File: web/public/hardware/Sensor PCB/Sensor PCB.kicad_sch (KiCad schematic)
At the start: 27 parts, among them J1 Conn_01x08_Pin, J2 Conn_01x08_Pin, J3 Conn_01x02_Pin, J4 Conn_01x02_Pin, U1 DRV5033AJxDBZ, U2 DRV5033AJxDBZ, U3 DRV5033AJxDBZ, U4 DRV5033AJxDBZ, U5 74LS11, U6 74LS11

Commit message: Fix routing to fit hall effect decoupling capacitors
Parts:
- added C3, C4, C5, C6: 0.1uF, Capacitor_SMD:C_0805_2012Metric_Pad1.18x1.45mm_HandSolder, symbol Device:C
- added H4: MountingHole, MountingHole:MountingHole_2.7mm_M2.5, symbol Mechanical:MountingHole
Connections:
- net +5V: now also C3.1, C4.1, C5.1, C6.1
- net GND: now also C3.2, C4.2, C5.2, C6.2
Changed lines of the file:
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@@
     (company "ECE 477")
   )
+  (junction (at 111.76 101.6) (diameter 0) (color 0 0 0 0)
+  )
+  (junction (at 60.96 55.88) (diameter 0) (color 0 0 0 0)
+  )
   (junction (at 237.49 120.65) (diameter 0) (color 0 0 0 0)
   )
@@
   (junction (at 123.19 111.76) (diameter 0) (color 0 0 0 0)
   )
+  (junction (at 59.69 101.6) (diameter 0) (color 0 0 0 0)
+  )
   (junction (at 237.49 146.05) (diameter 0) (color 0 0 0 0)
   )
@@
   )
   (junction (at 177.8 128.27) (diameter 0) (color 0 0 0 0)
+  )
+  (junction (at 110.49 55.88) (diameter 0) (color 0 0 0 0)
   )
   (junction (at 203.2 121.92) (diameter 0) (color 0 0 0 0)
@@
     (stroke (width 0) (type default))
   )
+  (wire (pts (xy 96.52 55.88) (xy 110.49 55.88))
+    (stroke (width 0) (type default))
+  )
   (wire (pts (xy 251.46 69.85) (xy 241.3 69.85))
     (stroke (width 0) (type default))
@@
     (stroke (width 0) (type default))
   )
+  (wire (pts (xy 45.72 101.6) (xy 59.69 101.6))
+    (stroke (width 0) (type default))
+  )
   (wire (pts (xy 123.19 66.04) (xy 123.19 81.28))
     (stroke (width 0) (type default))
@@
     (stroke (width 0) (type default))
   )
+  (wire (pts (xy 45.72 55.88) (xy 60.96 55.88))
+    (stroke (width 0) (type default))
+  )
   (wire (pts (xy 128.27 93.98) (xy 128.27 129.54))
     (stroke (width 0) (type default))
@@
   )
   (wire (pts (xy 69.85 111.76) (xy 69.85 93.98))
+    (stroke (width 0) (type default))
+  )
+  (wire (pts (xy 96.52 101.6) (xy 111.76 101.6))
     (stroke (width 0) (type default))
   )
@@
   (label "COL2_OUT" (at 153.67 81.28 0) (fields_autoplaced)
     (effects (font (size 1.27 1.27)) (justify left bottom))
+  )
+  (symbol (lib_id "power:GND") (at 96.52 109.22 0) (unit 1)
+    (in_bom yes) (on_board yes) (dnp no) (fields_autoplaced)
+    (property "Reference" "#PWR029" (at 96.52 115.57 0)
+      (effects (font (size 1.27 1.27)) hide)
+    )
+    (property "Value" "GND" (at 96.52 114.3 0)
+      (effects (font (size 1.27 1.27)) hide)
+    )
+    (property "Footprint" "" (at 96.52 109.22 0)
+      (effects (font (size 1.27 1.27)) hide)
+    )
+    (property "Datasheet" "" (at 96.52 109.22 0)
+      (effects (font (size 1.27 1.27)) hide)
+    )
+    (pin "1")
+    (instances
+      (project "Sensor PCB"
+        (path "/a9f063f9-73a8-44d6-aee6-f41a657d12c2"
+          (reference "#PWR029") (unit 1)
+        )
+      )
+    )
   )
   (symbol (lib_id "power:+5V") (at 73.66 55.88 0) (unit 1)
@@
     )
   )
+  (symbol (lib_id "Device:C") (at 45.72 59.69 0) (unit 1)
+    (in_bom yes) (on_board yes) (dnp no) (fields_autoplaced)
+    (property "Reference" "C4" (at 49.53 58.42 0)
+      (effects (font (size 1.27 1.27)) (justify left))
+    )
+    (property "Value" "0.1uF" (at 49.53 60.96 0)
+      (effects (font (size 1.27 1.27)) (justify left))
+    )
+    (property "Footprint" "Capacitor_SMD:C_0805_2012Metric_Pad1.18x1.45mm_HandSolder" (at 46.6852 63.5 0)
+      (effects (font (size 1.27 1.27)) hide)
+    )
+    (property "Datasheet" "~" (at 45.72 59.69 0)
+      (effects (font (size 1.27 1.27)) hide)
+    )
+    (pin "1")
+    (pin "2")
+    (instances
+      (project "Sensor PCB"
+        (path "/a9f063f9-73a8-44d6-aee6-f41a657d12c2"
+          (reference "C4") (unit 1)
+        )
+      )
+    )
+  )
   (symbol (lib_id "LED:WS2812B") (at 180.34 60.96 0) (unit 1)
     (in_bom yes) (on_board yes) (dnp no) (fields_autoplaced)
@@
         (path "/a9f063f9-73a8-44d6-aee6-f41a657d12c2"
           (reference "D1") (unit 1)
+        )
+      )
+    )
+  )
+  (symbol (lib_id "Device:C") (at 45.72 105.41 0) (unit 1)
+    (in_bom yes) (on_board yes) (dnp no) (fields_autoplaced)
+    (property "Reference" "C3" (at 49.53 104.14 0)
+      (effects (font (size 1.27 1.27)) (justify left))
+    )
+    (property "Value" "0.1uF" (at 49.53 106.68 0)
+      (effects (font (size 1.27 1.27)) (justify left))
+    )
+    (property "Footprint" "Capacitor_SMD:C_0805_2012Metric_Pad1.18x1.45mm_HandSolder" (at 46.6852 109.22 0)
+      (effects (font (size 1.27 1.27)) hide)
+    )
+    (property "Datasheet" "~" (at 45.72 105.41 0)
+      (effects (font (size 1.27 1.27)) hide)
+    )
+    (pin "1")
+    (pin "2")
+    (instances
+      (project "Sensor PCB"
+        (path "/a9f063f9-73a8-44d6-aee6-f41a657d12c2"
+          (reference "C3") (unit 1)
+        )
+      )
+    )
+  )
+  (symbol (lib_id "power:GND") (at 96.52 63.5 0) (unit 1)
+    (in_bom yes) (on_board yes) (dnp no) (fields_autoplaced)
+    (property "Reference" "#PWR040" (at 96.52 69.85 0)
+      (effects (font (size 1.27 1.27)) hide)
+    )
+    (property "Value" "GND" (at 96.52 68.58 0)
+      (effects (font (size 1.27 1.27)) hide)
+    )
+    (property "Footprint" "" (at 96.52 63.5 0)
+      (effects (font (size 1.27 1.27)) hide)
+    )
+    (property "Datasheet" "" (at 96.52 63.5 0)
+      (effects (font (size 1.27 1.27)) hide)
+    )
+    (pin "1")
+    (instances
+      (project "Sensor PCB"
+        (path "/a9f063f9-73a8-44d6-aee6-f41a657d12c2"
+          (reference "#PWR040") (unit 1)
         )
       )
@@
     )
   )
+  (symbol (lib_id "Mechanical:MountingHole") (at 38.1 191.77 0) (unit 1)
+    (in_bom yes) (on_board yes) (dnp no) (fields_autoplaced)
+    (property "Reference" "H4" (at 40.64 190.5 0)
+      (effects (font (size 1.27 1.27)) (justify left))
+    )
+    (property "Value" "MountingHole" (at 40.64 193.04 0)
+      (effects (font (size 1.27 1.27)) (justify left))
+    )
+    (property "Footprint" "MountingHole:MountingHole_2.7mm_M2.5" (at 38.1 191.77 0)
+      (effects (font (size 1.27 1.27)) hide)
+    )
+    (property "Datasheet" "~" (at 38.1 191.77 0)
+      (effects (font (size 1.27 1.27)) hide)
+    )
+    (instances
+      (project "Sensor PCB"
+        (path "/a9f063f9-73a8-44d6-aee6-f41a657d12c2"
+          (reference "H4") (unit 1)
+        )
+      )
+    )
+  )
+  (symbol (lib_id "power:GND") (at 45.72 63.5 0) (unit 1)
+    (in_bom yes) (on_board yes) (dnp no) (fields_autoplaced)
+    (property "Reference" "#PWR039" (at 45.72 69.85 0)
+      (effects (font (size 1.27 1.27)) hide)
+    )
+    (property "Value" "GND" (at 45.72 68.58 0)
+      (effects (font (size 1.27 1.27)) hide)
+    )
+    (property "Footprint" "" (at 45.72 63.5 0)
+      (effects (font (size 1.27 1.27)) hide)
+    )
+    (property "Datasheet" "" (at 45.72 63.5 0)
+      (effects (font (size 1.27 1.27)) hide)
+    )
+    (pin "1")
+    (instances
+      (project "Sensor PCB"
+        (path "/a9f063f9-73a8-44d6-aee6-f41a657d12c2"
+          (reference "#PWR039") (unit 1)
+        )
+      )
+    )
+  )
   (symbol (lib_id "power:+5V") (at 110.49 55.88 0) (unit 1)
     (in_bom yes) (on_board yes) (dnp no) (fields_autoplaced)
@@
     )
   )
+  (symbol (lib_id "Device:C") (at 96.52 59.69 0) (unit 1)
+    (in_bom yes) (on_board yes) (dnp no) (fields_autoplaced)
+    (property "Reference" "C5" (at 100.33 58.42 0)
+      (effects (font (size 1.27 1.27)) (justify left))
+    )
+    (property "Value" "0.1uF" (at 100.33 60.96 0)
+      (effects (font (size 1.27 1.27)) (justify left))
+    )
+    (property "Footprint" "Capacitor_SMD:C_0805_2012Metric_Pad1.18x1.45mm_HandSolder" (at 97.4852 63.5 0)
+      (effects (font (size 1.27 1.27)) hide)
+    )
+    (property "Datasheet" "~" (at 96.52 59.69 0)
+      (effects (font (size 1.27 1.27)) hide)
+    )
+    (pin "1")
+    (pin "2")
+    (instances
+      (project "Sensor PCB"
+        (path "/a9f063f9-73a8-44d6-aee6-f41a657d12c2"
+          (reference "C5") (unit 1)
+        )
+      )
+    )
+  )
   (symbol (lib_id "power:+5V") (at 251.46 59.69 90) (mirror x) (unit 1)
     (in_bom yes) (on_board yes) (dnp no) (fields_autoplaced)
@@
     )
   )
+  (symbol (lib_id "power:GND") (at 45.72 109.22 0) (unit 1)
+    (in_bom yes) (on_board yes) (dnp no) (fields_autoplaced)
+    (property "Reference" "#PWR030" (at 45.72 115.57 0)
+      (effects (font (size 1.27 1.27)) hide)
+    )
+    (property "Value" "GND" (at 45.72 114.3 0)
+      (effects (font (size 1.27 1.27)) hide)
+    )
+    (property "Footprint" "" (at 45.72 109.22 0)
+      (effects (font (size 1.27 1.27)) hide)
+    )
+    (property "Datasheet" "" (at 45.72 109.22 0)
+      (effects (font (size 1.27 1.27)) hide)
+    )
+    (pin "1")
+    (instances
+      (project "Sensor PCB"
+        (path "/a9f063f9-73a8-44d6-aee6-f41a657d12c2"
+          (reference "#PWR030") (unit 1)
+        )
+      )
+    )
+  )
   (symbol (lib_id "power:GND") (at 60.96 76.2 0) (unit 1)
     (in_bom yes) (on_board yes) (dnp no) (fields_autoplaced)
@@
         )
       )
+    )
+  )
+  (symbol (lib_id "Device:C") (at 96.52 105.41 0) (unit 1)
+    (in_bom yes) (on_board yes) (dnp no) (fields_autoplaced)
+    (property "Reference" "C6" (at 100.33 104.14 0)
+      (effects (font (size 1.27 1.27)) (justify left))
+    )
+    (property "Value" "0.1uF" (at 100.33 106.68 0)
+      (effects (font (size 1.27 1.27)) (justify left))
+    )
+    (property "Footprint" "Capacitor_SMD:C_0805_2012Metric_Pad1.18x1.45mm_HandSolder" (at 97.4852 109.22 0)
+      (effects (font (size 1.27 1.27)) hide)
+    )
+    (property "Datasheet" "~" (at 96.52 105.41 0)
+      (effects (font (size 1.27 1.27)) hide)
+    )
+    (pin "1")
+    (pin "2")
+    (instances
+      (project "Sensor PCB"
+        (path "/a9f063f9-73a8-44d6-aee6-f41a657d12c2"
+          (reference "C6") (unit 1)
+        )
+      )

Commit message: Flip LED2 signal direction
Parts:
- renumbered D4 to D3, D3 to D4
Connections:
- net LED2_IN: now also J2.4 (Pin_4); no longer J1.5 (Pin_5)
- net LED2_OUT: now also J1.5 (Pin_5); no longer J2.4 (Pin_4)
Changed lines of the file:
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@@
     (effects (font (size 1.27 1.27)) (justify right bottom))
   )
-  (label "LED2_OUT" (at 241.3 67.31 180) (fields_autoplaced)
+  (label "LED2_OUT" (at 33.02 87.63 0) (fields_autoplaced)
+    (effects (font (size 1.27 1.27)) (justify left bottom))
+  )
+  (label "LED2_IN" (at 241.3 67.31 180) (fields_autoplaced)
     (effects (font (size 1.27 1.27)) (justify right bottom))
-  )
-  (label "LED2_IN" (at 33.02 87.63 0) (fields_autoplaced)
-    (effects (font (size 1.27 1.27)) (justify left bottom))
   )
   (label "COL1_OUT" (at 125.73 148.59 90) (fields_autoplaced)
@@
   (symbol (lib_id "LED:WS2812B") (at 208.28 93.98 0) (unit 1)
     (in_bom yes) (on_board yes) (dnp no) (fields_autoplaced)
-    (property "Reference" "D4" (at 219.71 90.3321 0)
+    (property "Reference" "D3" (at 219.71 90.3321 0)
       (effects (font (size 1.27 1.27)))
     )
@@
       (project "Sensor PCB"
         (path "/a9f063f9-73a8-44d6-aee6-f41a657d12c2"
-          (reference "D4") (unit 1)
+          (reference "D3") (unit 1)
         )
       )
@@
   (symbol (lib_id "LED:WS2812B") (at 180.34 93.98 0) (unit 1)
     (in_bom yes) (on_board yes) (dnp no) (fields_autoplaced)
-    (property "Reference" "D3" (at 191.77 90.3321 0)
+    (property "Reference" "D4" (at 191.77 90.3321 0)
       (effects (font (size 1.27 1.27)))
     )
@@
       (project "Sensor PCB"
         (path "/a9f063f9-73a8-44d6-aee6-f41a657d12c2"
-          (reference "D3") (unit 1)
-        )
-      )
+          (reference "D4") (unit 1)
+        )
+      )

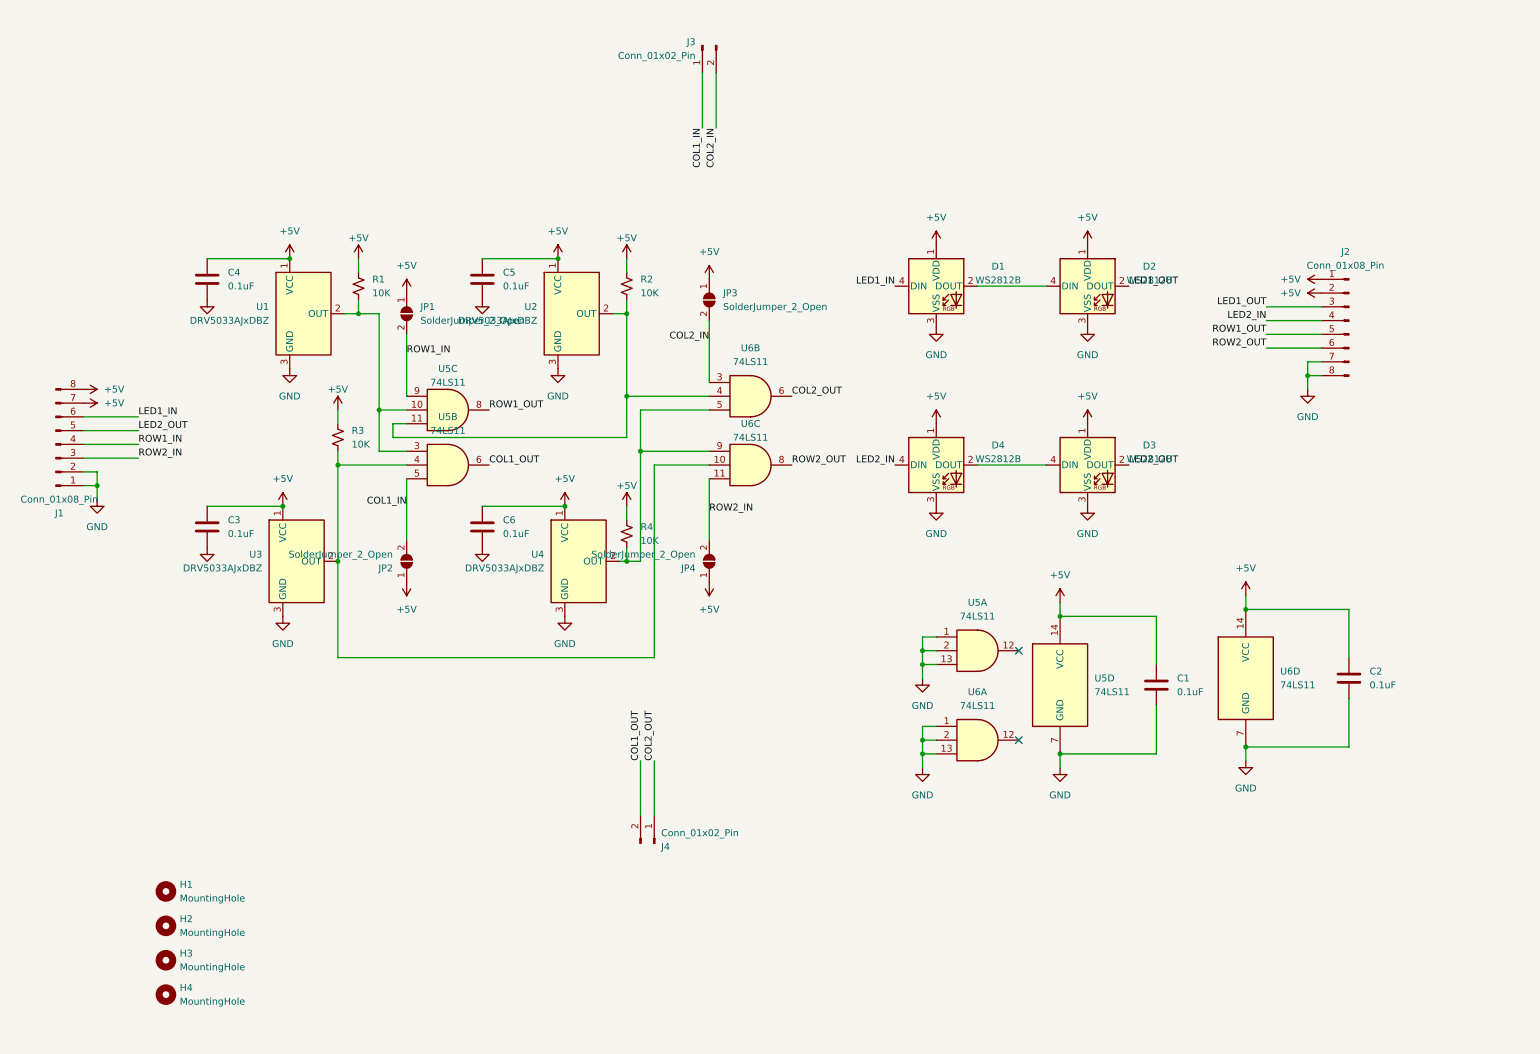
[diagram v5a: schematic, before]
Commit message: Grouped Connectors, LEDs, and Mounting Holes
Each were group separately
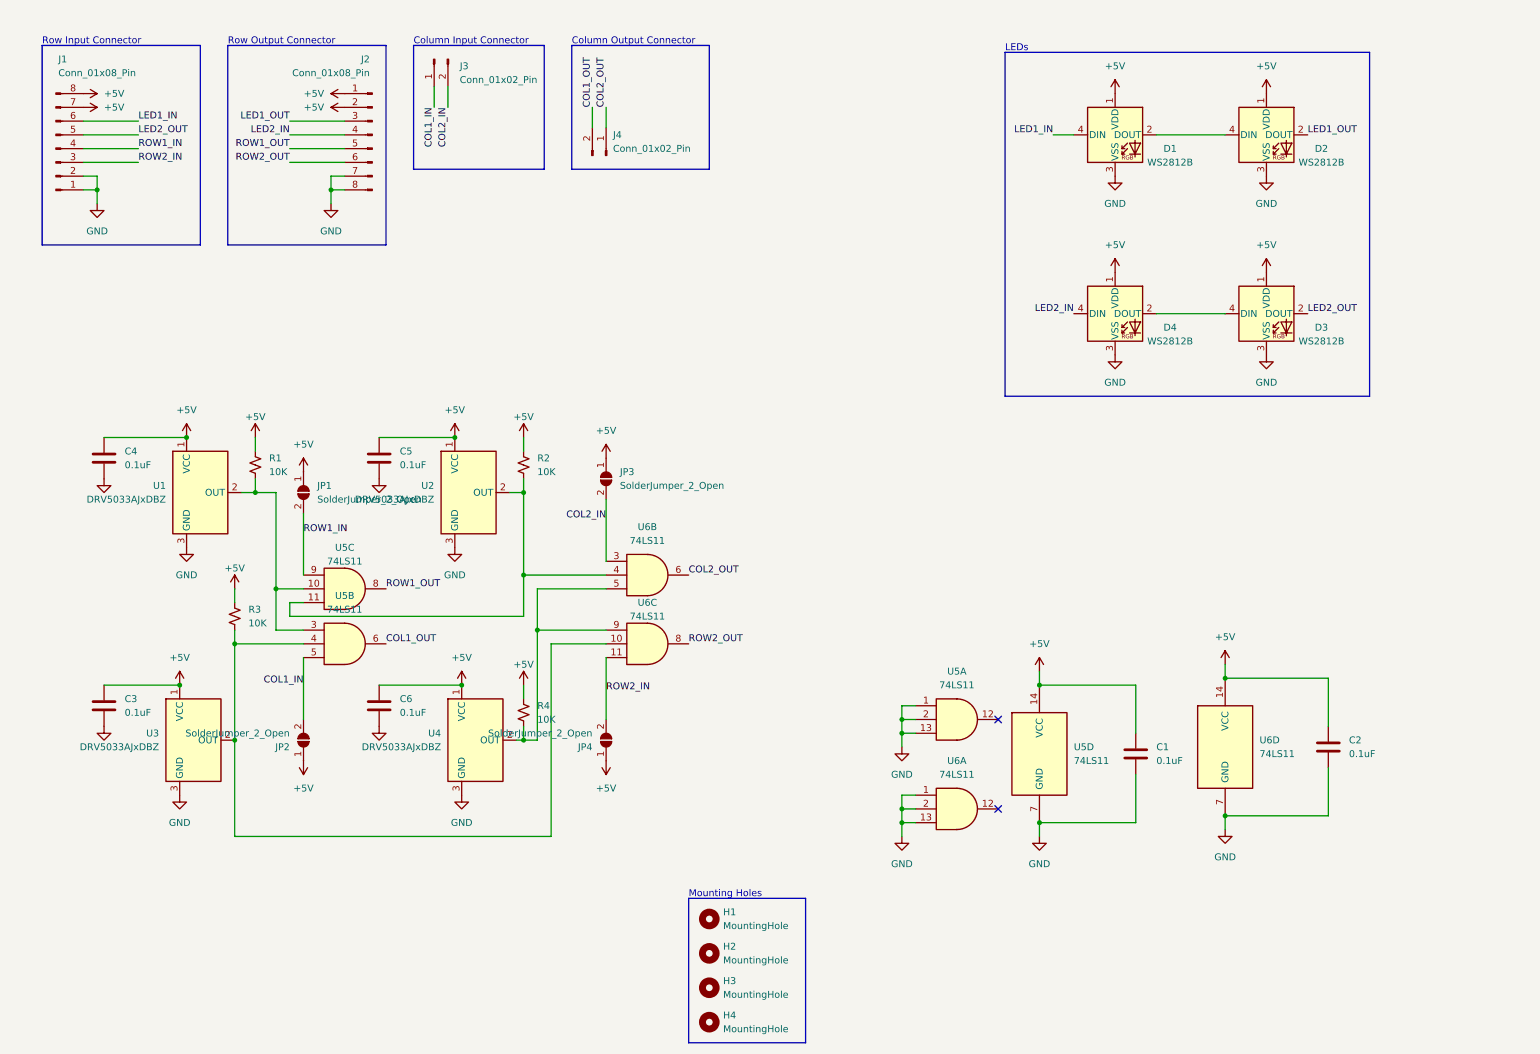
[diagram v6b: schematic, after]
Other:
- note added: "Column Input Connector"
- note added: "Column Output Connector"
- note added: "LEDs"
- note added: "Mounting Holes"
- note added: "Row Input Connector"
- note added: "Row Output Connector"
- moved on the sheet: C1, C2, C3, C4, C5, C6, D1, D2, D3, D4, H1, H2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

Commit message: Updated component names
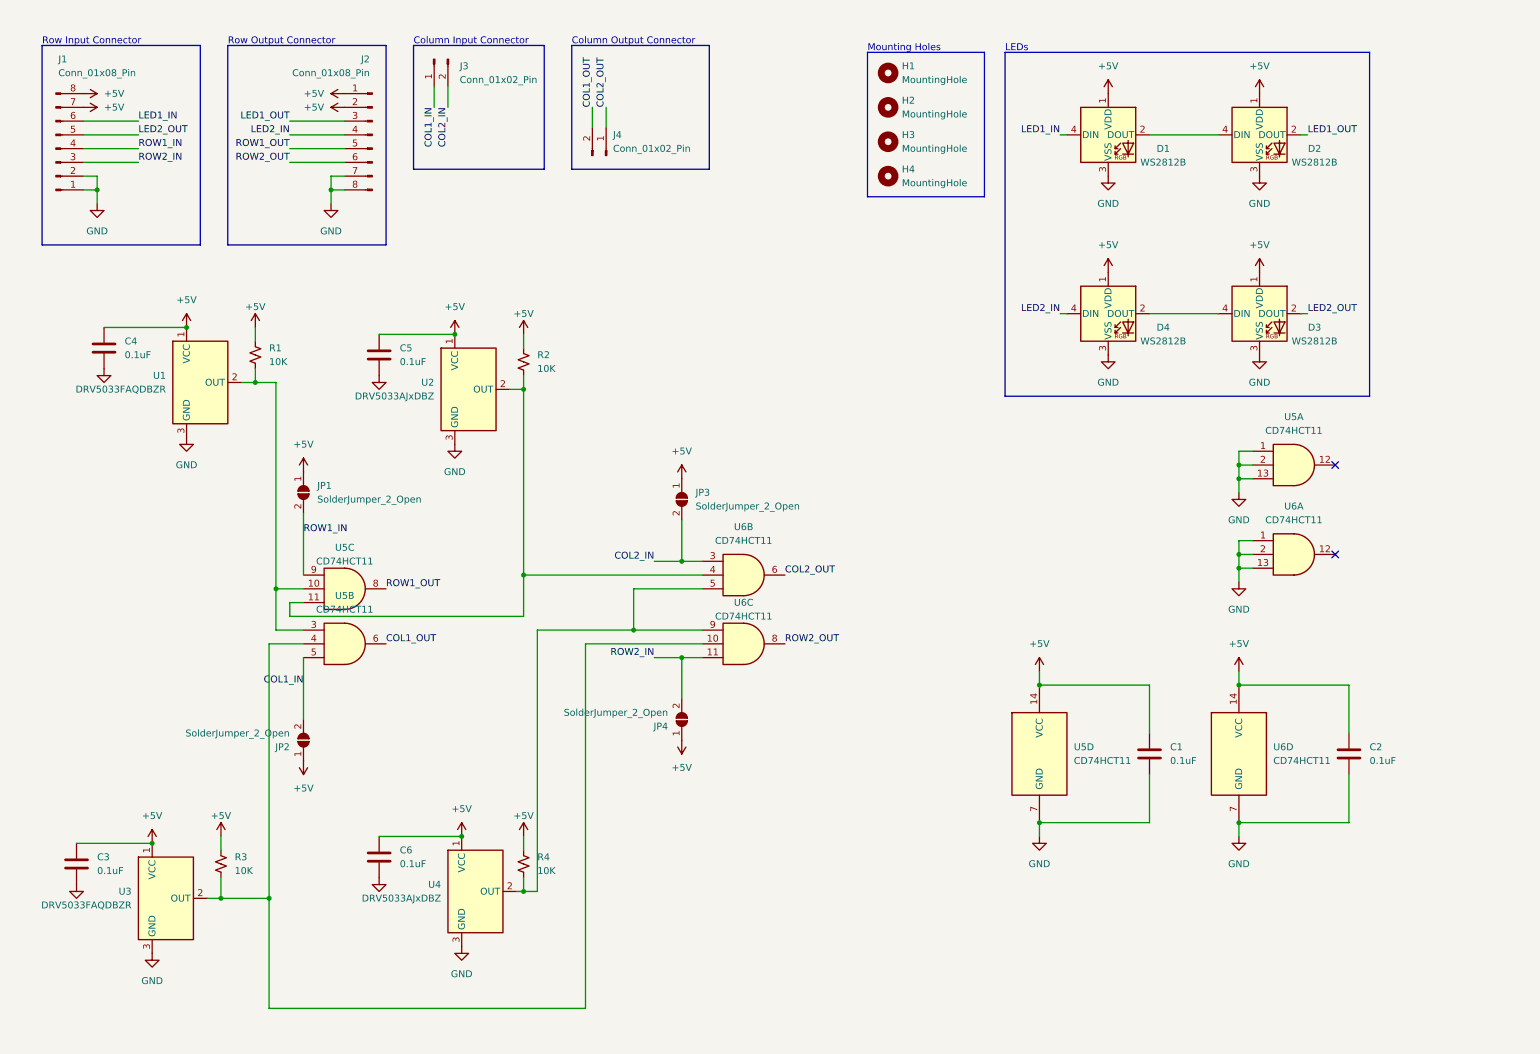
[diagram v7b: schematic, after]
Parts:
- U1, U3: value DRV5033AJxDBZ -> DRV5033FAQDBZR
- U5, U6: value 74LS11 -> CD74HCT11
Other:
- moved on the sheet: C1, C2, C3, C4, C5, C6, D1, D2, D3, D4, H1, H2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
